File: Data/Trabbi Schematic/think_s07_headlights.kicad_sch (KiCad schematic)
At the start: 12 parts, among them K1 DRL Relay R5, K2 Park Light Relay R17, SW1 Headlight Switch (C25)

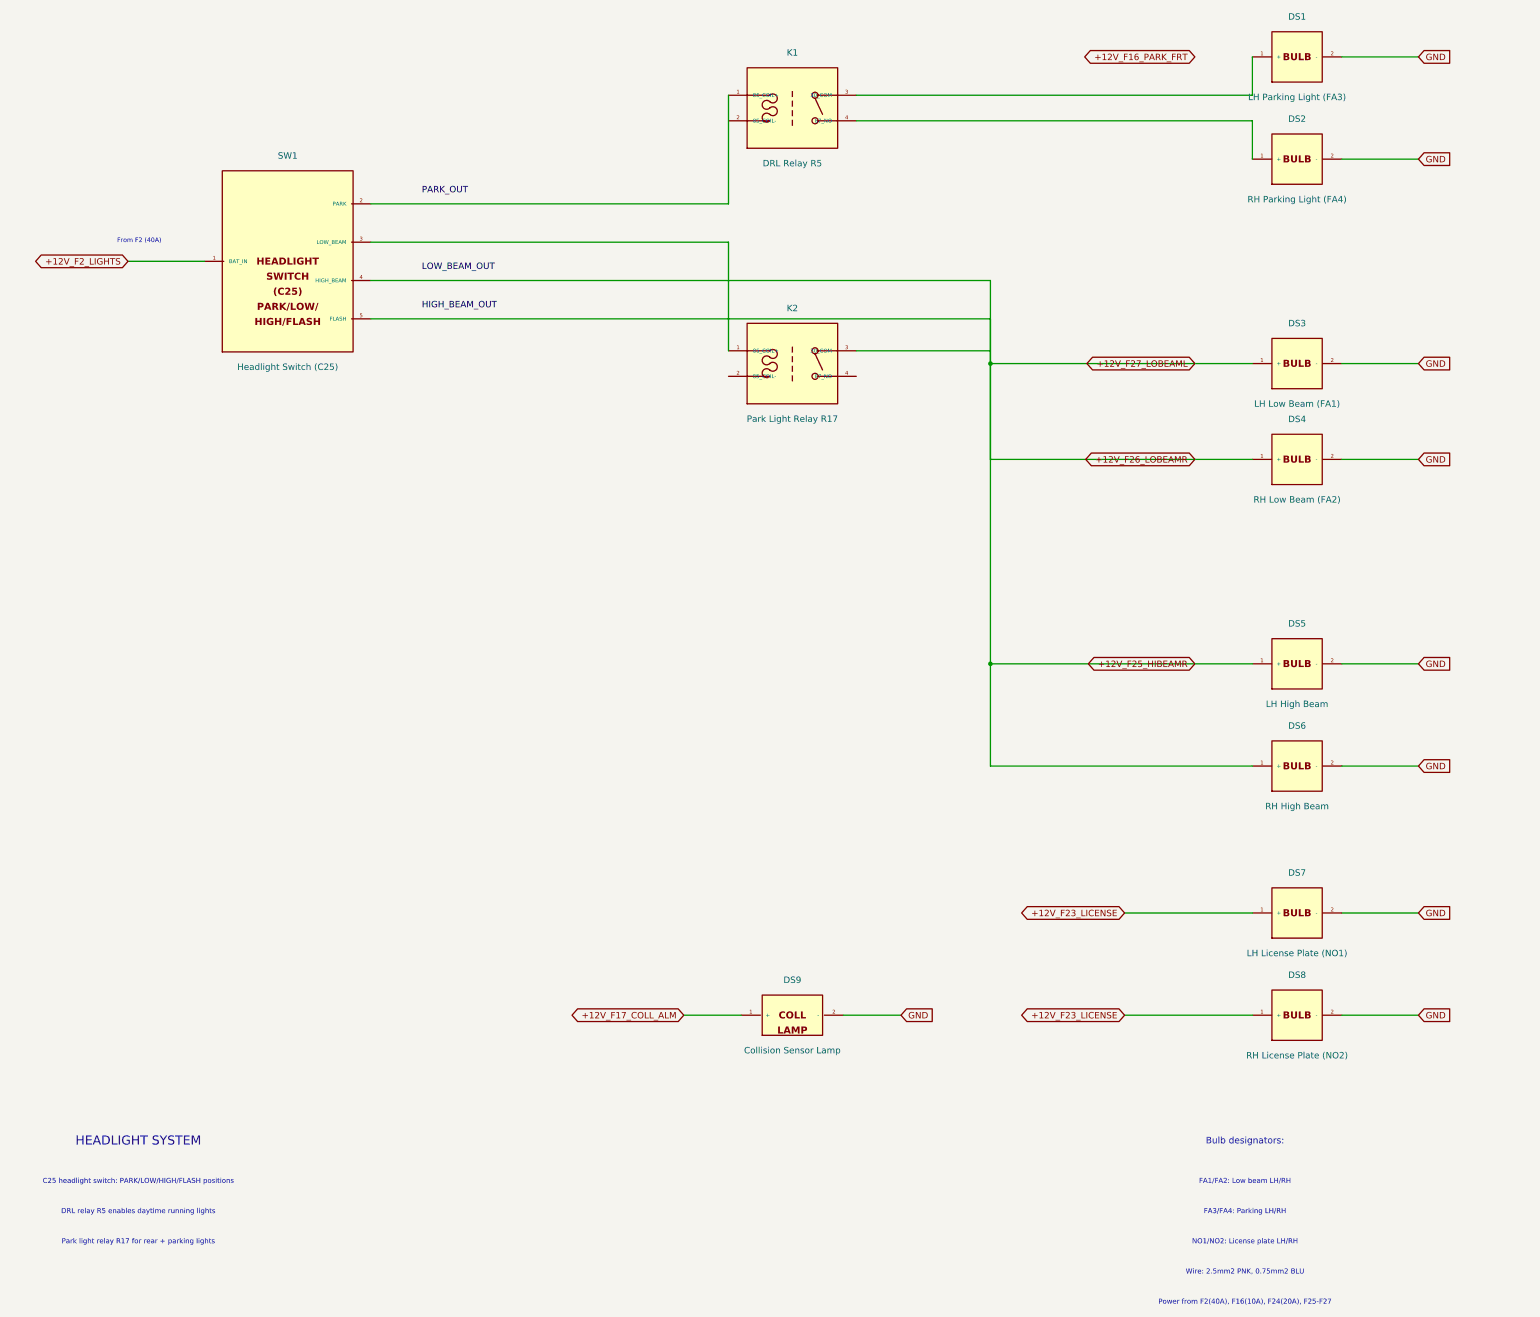
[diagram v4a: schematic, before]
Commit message: Add cross-sheet reference annotations to global labels
- Track all global label positions per sheet during build
- After building all sheets, annotate each global label with
  "→S01,S03,..." text showing which other sheets share the net
- 60 cross-sheet nets identified and annotated
- Two-pass build: 1) build all sheets 2) add cross-refs + save
- Text placed near label in 0.8mm font, offset to avoid overlap

Co-Authored-By: Claude Opus 4.6 <noreply@anthropic.com>
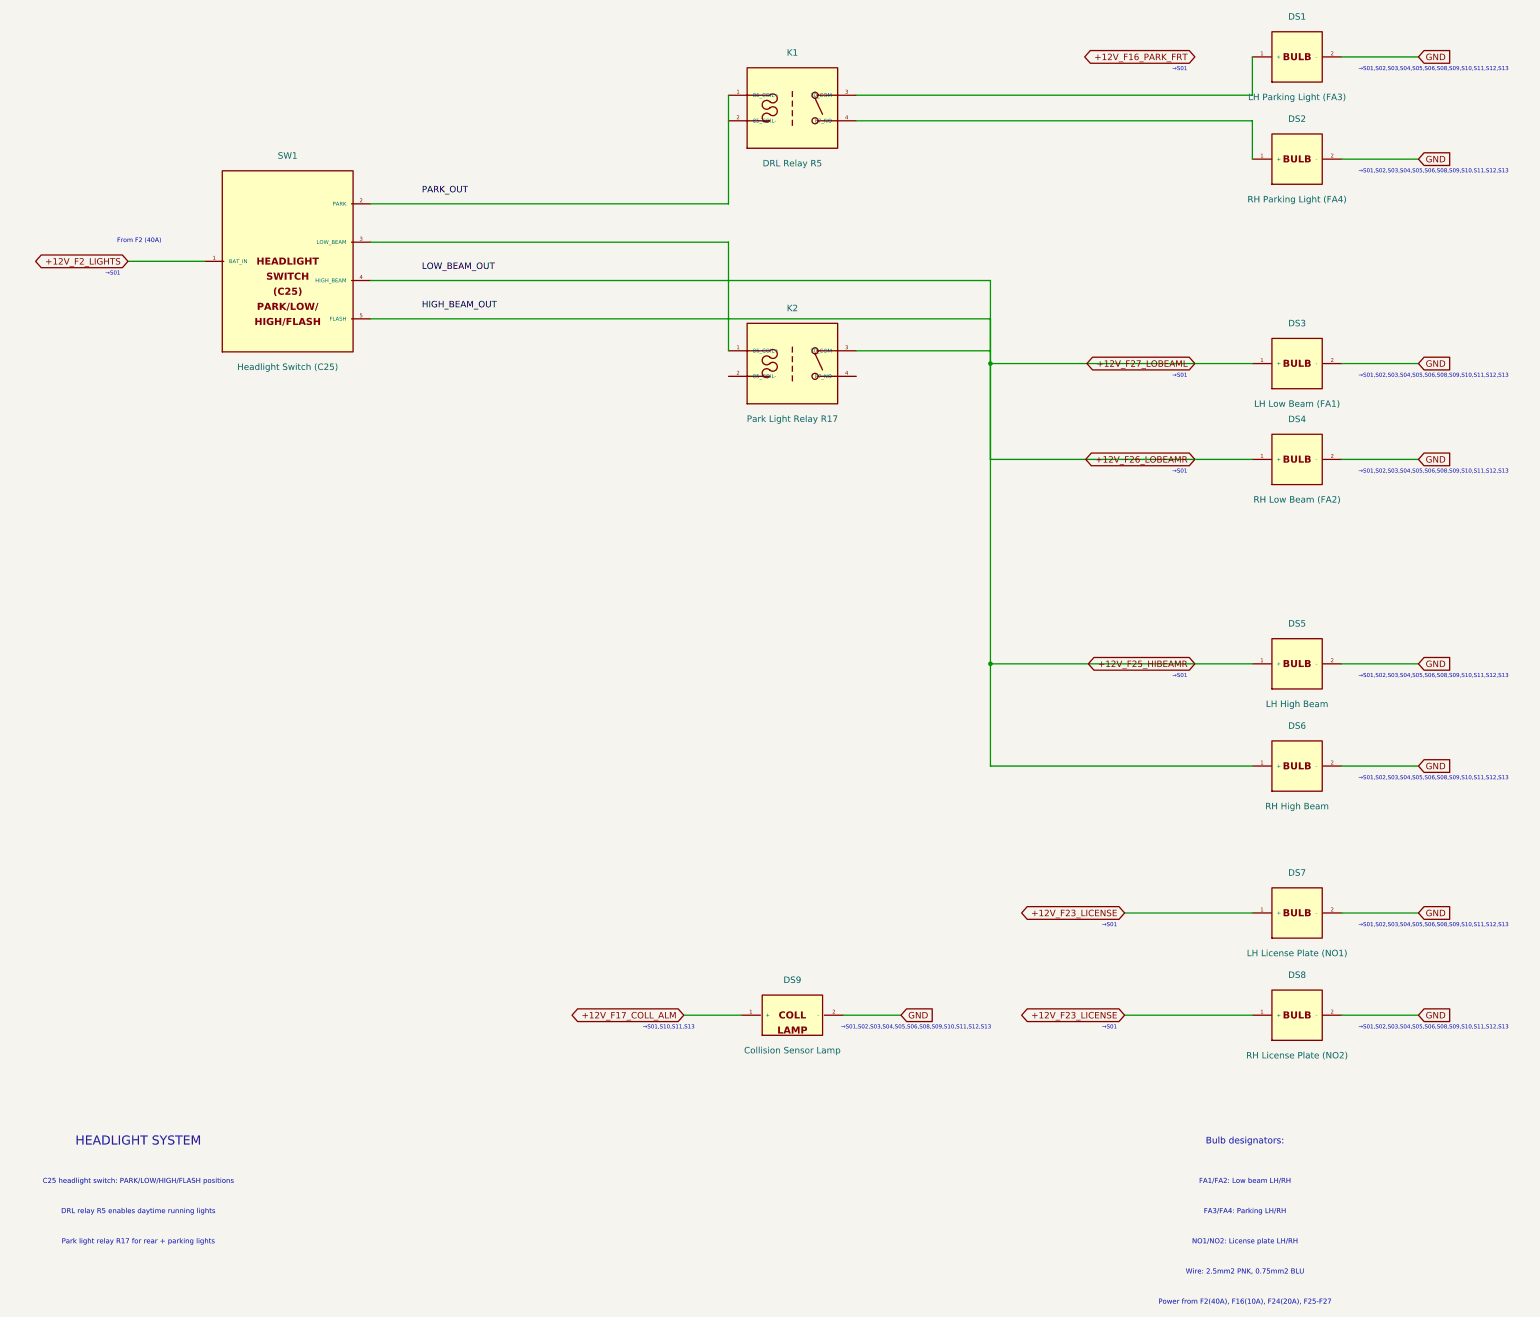
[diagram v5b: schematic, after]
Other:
- note added: "→S01"
- note added: "→S01,S02,S03,S04,S05,S06,S08,S09,S10,S11,S12,S13"
- note added: "→S01,S10,S11,S13"
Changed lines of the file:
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@@
     (effects (font (size 1.000 1.000)))
+  )
+  (text "→S01" (at 24.940 82.510 0)
+    (effects (font (size 0.800 0.800)))
+  )
+  (text "→S01,S02,S03,S04,S05,S06,S08,S09,S10,S11,S12,S13" (at 287.480 41.870 0)
+    (effects (font (size 0.800 0.800)))
+  )
+  (text "→S01,S02,S03,S04,S05,S06,S08,S09,S10,S11,S12,S13" (at 287.480 62.190 0)
+    (effects (font (size 0.800 0.800)))
+  )
+  (text "→S01,S02,S03,S04,S05,S06,S08,S09,S10,S11,S12,S13" (at 287.480 102.830 0)
+    (effects (font (size 0.800 0.800)))
+  )
+  (text "→S01,S02,S03,S04,S05,S06,S08,S09,S10,S11,S12,S13" (at 287.480 121.880 0)
+    (effects (font (size 0.800 0.800)))
+  )
+  (text "→S01,S02,S03,S04,S05,S06,S08,S09,S10,S11,S12,S13" (at 287.480 162.520 0)
+    (effects (font (size 0.800 0.800)))
+  )
+  (text "→S01,S02,S03,S04,S05,S06,S08,S09,S10,S11,S12,S13" (at 287.480 182.840 0)
+    (effects (font (size 0.800 0.800)))
+  )
+  (text "→S01,S02,S03,S04,S05,S06,S08,S09,S10,S11,S12,S13" (at 287.480 212.050 0)
+    (effects (font (size 0.800 0.800)))
+  )
+  (text "→S01,S02,S03,S04,S05,S06,S08,S09,S10,S11,S12,S13" (at 287.480 232.370 0)
+    (effects (font (size 0.800 0.800)))
+  )
+  (text "→S01,S02,S03,S04,S05,S06,S08,S09,S10,S11,S12,S13" (at 184.610 232.370 0)
+    (effects (font (size 0.800 0.800)))
+  )
+  (text "→S01" (at 223.060 212.050 0)
+    (effects (font (size 0.800 0.800)))
+  )
+  (text "→S01" (at 223.060 232.370 0)
+    (effects (font (size 0.800 0.800)))
+  )
+  (text "→S01" (at 237.030 41.870 0)
+    (effects (font (size 0.800 0.800)))
+  )
+  (text "→S01" (at 237.030 102.830 0)
+    (effects (font (size 0.800 0.800)))
+  )
+  (text "→S01" (at 237.030 121.880 0)
+    (effects (font (size 0.800 0.800)))
+  )
+  (text "→S01" (at 237.030 162.520 0)
+    (effects (font (size 0.800 0.800)))
+  )
+  (text "→S01,S10,S11,S13" (at 135.430 232.370 0)
+    (effects (font (size 0.800 0.800)))
   )
   (symbol_instances)

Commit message: Fix label text justification for KiCad 9
Add (justify left) to all label and global_label effects.
KiCad 9 requires explicit text justification — without it,
label text is mispositioned relative to the label shape.

Co-Authored-By: Claude Opus 4.6 <noreply@anthropic.com>
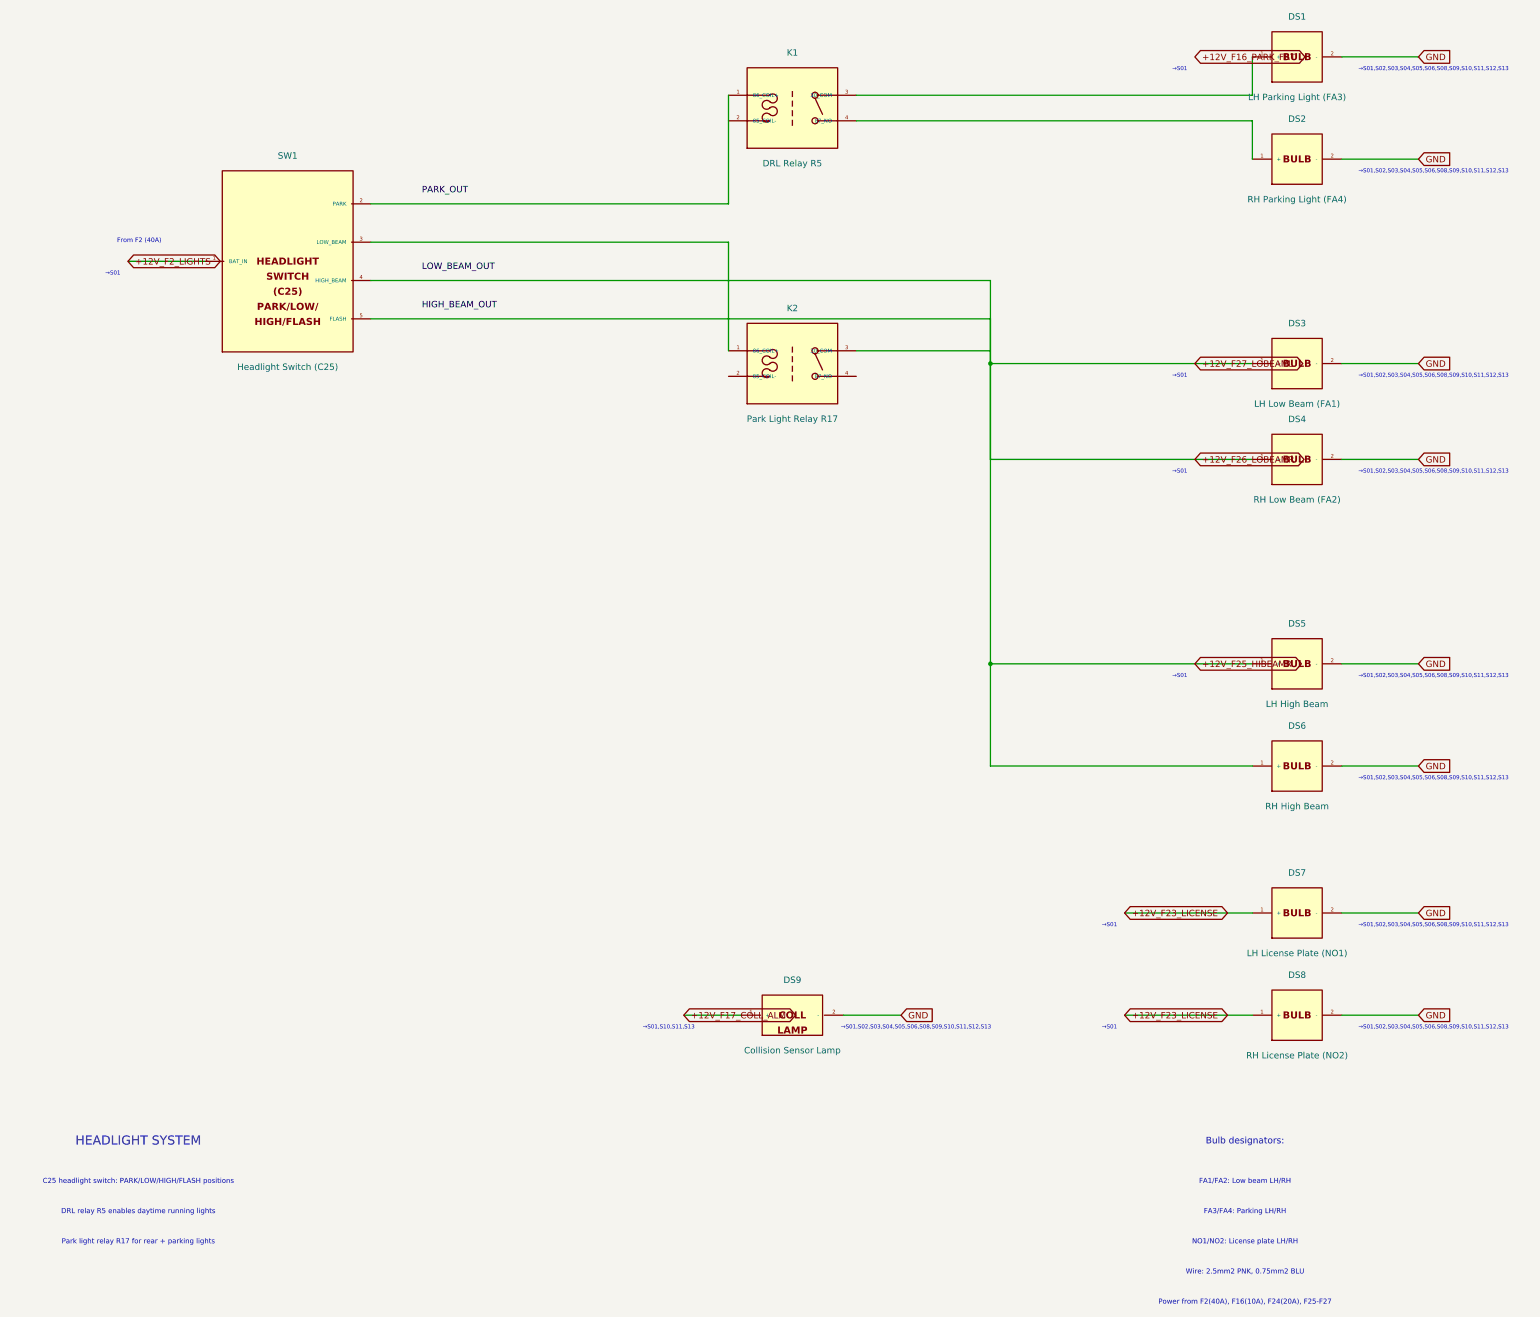
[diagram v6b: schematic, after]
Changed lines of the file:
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@@
   )
   (global_label "+12V_F2_LIGHTS" (shape bidirectional) (at 27.940 80.010 180)
-    (effects (font (size 1.27 1.27)))
+    (effects (font (size 1.27 1.27)) (justify left))
     (property "Intersheetrefs" "${INTERSHEET_REFS}" (at 27.940 80.010 0)
       (effects (font (size 1.27 1.27)) hide)
@@
   )
   (label "PARK_OUT" (at 86.360 66.040 0)
-    (effects (font (size 1.27 1.27)))
+    (effects (font (size 1.27 1.27)) (justify left))
   )
   (wire (pts (xy 76.200 76.200) (xy 147.320 76.200))
@@
   )
   (label "LOW_BEAM_OUT" (at 86.360 81.280 0)
-    (effects (font (size 1.27 1.27)))
+    (effects (font (size 1.27 1.27)) (justify left))
   )
   (wire (pts (xy 76.200 91.440) (xy 199.390 91.440))
@@
   )
   (label "HIGH_BEAM_OUT" (at 86.360 88.900 0)
-    (effects (font (size 1.27 1.27)))
+    (effects (font (size 1.27 1.27)) (justify left))
   )
   (wire (pts (xy 172.720 46.990) (xy 251.460 46.990))
@@
   )
   (global_label "GND" (shape input) (at 284.480 39.370 0)
-    (effects (font (size 1.27 1.27)))
+    (effects (font (size 1.27 1.27)) (justify left))
     (property "Intersheetrefs" "${INTERSHEET_REFS}" (at 284.480 39.370 0)
       (effects (font (size 1.27 1.27)) hide)
@@
   )
   (global_label "GND" (shape input) (at 284.480 59.690 0)
-    (effects (font (size 1.27 1.27)))
+    (effects (font (size 1.27 1.27)) (justify left))
     (property "Intersheetrefs" "${INTERSHEET_REFS}" (at 284.480 59.690 0)
       (effects (font (size 1.27 1.27)) hide)
@@
   )
   (global_label "GND" (shape input) (at 284.480 100.330 0)
-    (effects (font (size 1.27 1.27)))
+    (effects (font (size 1.27 1.27)) (justify left))
     (property "Intersheetrefs" "${INTERSHEET_REFS}" (at 284.480 100.330 0)
       (effects (font (size 1.27 1.27)) hide)
@@
   )
   (global_label "GND" (shape input) (at 284.480 119.380 0)
-    (effects (font (size 1.27 1.27)))
+    (effects (font (size 1.27 1.27)) (justify left))
     (property "Intersheetrefs" "${INTERSHEET_REFS}" (at 284.480 119.380 0)
       (effects (font (size 1.27 1.27)) hide)
@@
   )
   (global_label "GND" (shape input) (at 284.480 160.020 0)
-    (effects (font (size 1.27 1.27)))
+    (effects (font (size 1.27 1.27)) (justify left))
     (property "Intersheetrefs" "${INTERSHEET_REFS}" (at 284.480 160.020 0)
       (effects (font (size 1.27 1.27)) hide)
@@
   )
   (global_label "GND" (shape input) (at 284.480 180.340 0)
-    (effects (font (size 1.27 1.27)))
+    (effects (font (size 1.27 1.27)) (justify left))
     (property "Intersheetrefs" "${INTERSHEET_REFS}" (at 284.480 180.340 0)
       (effects (font (size 1.27 1.27)) hide)
@@
   )
   (global_label "GND" (shape input) (at 284.480 209.550 0)
-    (effects (font (size 1.27 1.27)))
+    (effects (font (size 1.27 1.27)) (justify left))
     (property "Intersheetrefs" "${INTERSHEET_REFS}" (at 284.480 209.550 0)
       (effects (font (size 1.27 1.27)) hide)
@@
   )
   (global_label "GND" (shape input) (at 284.480 229.870 0)
-    (effects (font (size 1.27 1.27)))
+    (effects (font (size 1.27 1.27)) (justify left))
     (property "Intersheetrefs" "${INTERSHEET_REFS}" (at 284.480 229.870 0)
       (effects (font (size 1.27 1.27)) hide)
@@
   )
   (global_label "+12V_F23_LICENSE" (shape bidirectional) (at 226.060 209.550 180)
-    (effects (font (size 1.27 1.27)))
+    (effects (font (size 1.27 1.27)) (justify left))
     (property "Intersheetrefs" "${INTERSHEET_REFS}" (at 226.060 209.550 0)
       (effects (font (size 1.27 1.27)) hide)
@@
   )
   (global_label "+12V_F23_LICENSE" (shape bidirectional) (at 226.060 229.870 180)
-    (effects (font (size 1.27 1.27)))
+    (effects (font (size 1.27 1.27)) (justify left))
     (property "Intersheetrefs" "${INTERSHEET_REFS}" (at 226.060 229.870 0)
       (effects (font (size 1.27 1.27)) hide)
@@
   )
   (global_label "+12V_F16_PARK_FRT" (shape bidirectional) (at 240.030 39.370 180)
-    (effects (font (size 1.27 1.27)))
+    (effects (font (size 1.27 1.27)) (justify left))
     (property "Intersheetrefs" "${INTERSHEET_REFS}" (at 240.030 39.370 0)
       (effects (font (size 1.27 1.27)) hide)
@@
   )
   (global_label "+12V_F27_LOBEAML" (shape bidirectional) (at 240.030 100.330 180)
-    (effects (font (size 1.27 1.27)))
+    (effects (font (size 1.27 1.27)) (justify left))
     (property "Intersheetrefs" "${INTERSHEET_REFS}" (at 240.030 100.330 0)
       (effects (font (size 1.27 1.27)) hide)
@@
   )
   (global_label "+12V_F26_LOBEAMR" (shape bidirectional) (at 240.030 119.380 180)
-    (effects (font (size 1.27 1.27)))
+    (effects (font (size 1.27 1.27)) (justify left))
     (property "Intersheetrefs" "${INTERSHEET_REFS}" (at 240.030 119.380 0)
       (effects (font (size 1.27 1.27)) hide)
@@
   )
   (global_label "+12V_F25_HIBEAMR" (shape bidirectional) (at 240.030 160.020 180)
-    (effects (font (size 1.27 1.27)))
+    (effects (font (size 1.27 1.27)) (justify left))
     (property "Intersheetrefs" "${INTERSHEET_REFS}" (at 240.030 160.020 0)
       (effects (font (size 1.27 1.27)) hide)
@@
   )
   (global_label "+12V_F17_COLL_ALM" (shape bidirectional) (at 138.430 229.870 180)
-    (effects (font (size 1.27 1.27)))
+    (effects (font (size 1.27 1.27)) (justify left))
     (property "Intersheetrefs" "${INTERSHEET_REFS}" (at 138.430 229.870 0)
       (effects (font (size 1.27 1.27)) hide)
@@
   )
   (global_label "GND" (shape input) (at 181.610 229.870 0)
-    (effects (font (size 1.27 1.27)))
+    (effects (font (size 1.27 1.27)) (justify left))
     (property "Intersheetrefs" "${INTERSHEET_REFS}" (at 181.610 229.870 0)
       (effects (font (size 1.27 1.27)) hide)
